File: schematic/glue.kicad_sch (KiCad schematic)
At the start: 1 part

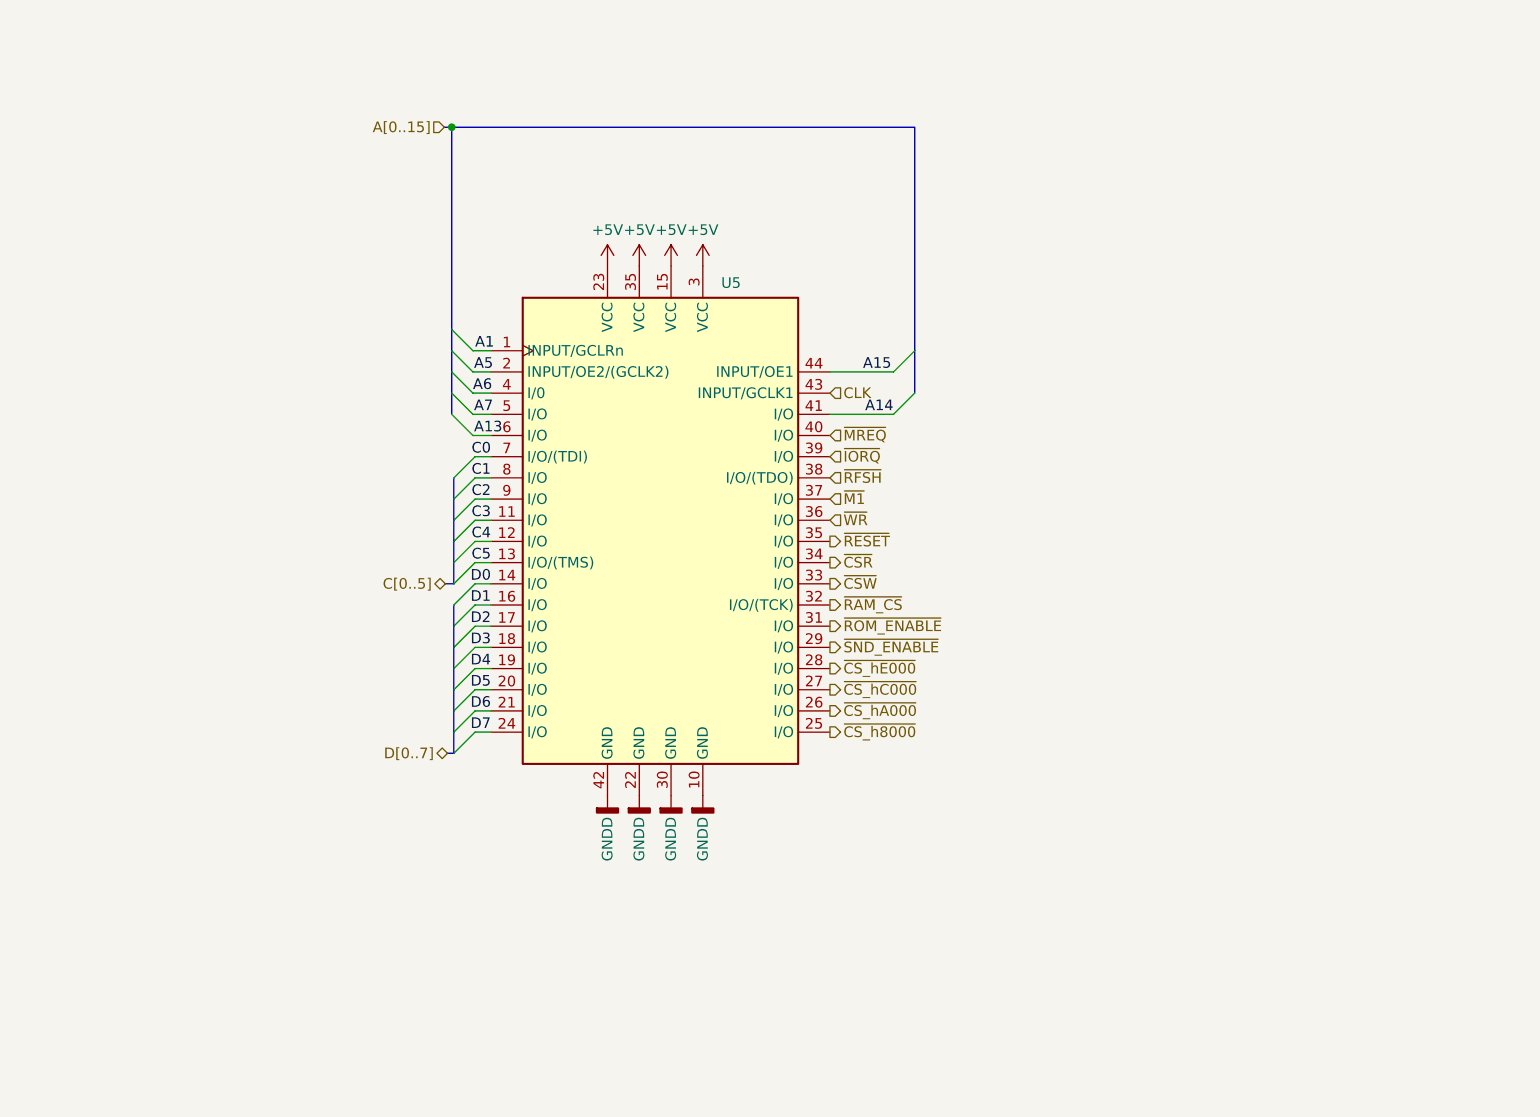
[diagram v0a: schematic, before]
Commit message: first commit of portable coleco, major changes... pcb meh. CPLD code tested, quartus build works.
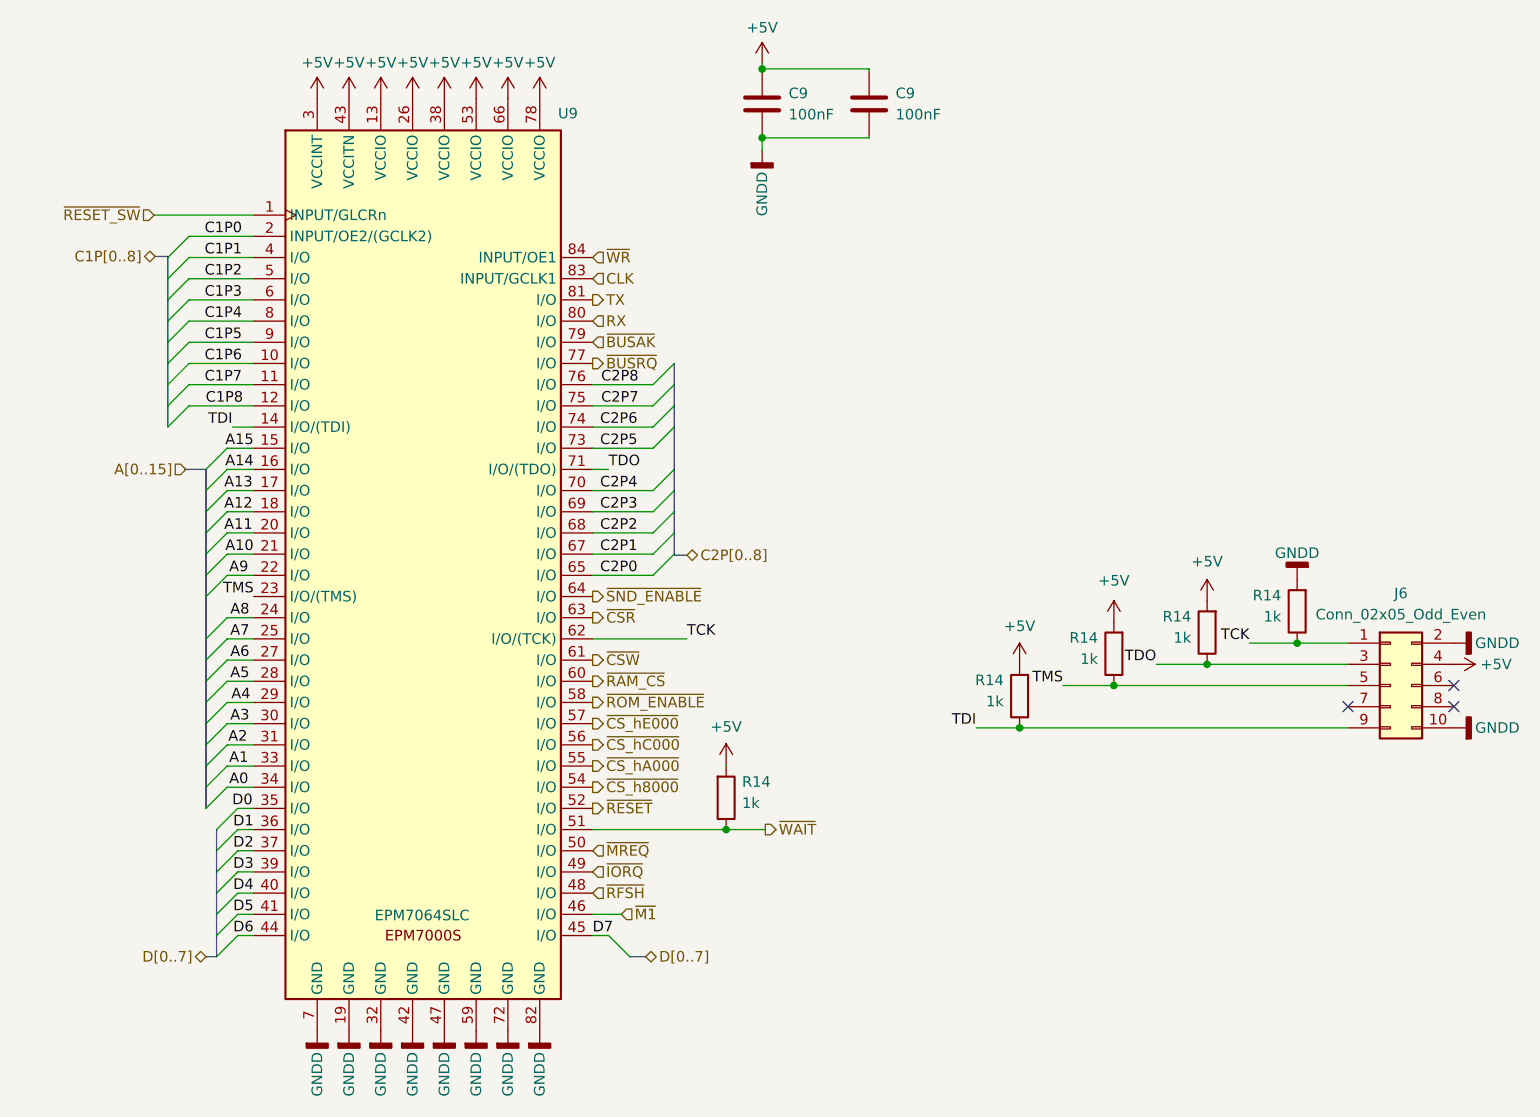
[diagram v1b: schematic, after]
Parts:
- removed U5: ~, symbol CPLD:MAX7000_44_PLC
- added C9 (x2): 100nF, Capacitor_THT:C_Disc_D7.0mm_W2.5mm_P5.00mm, symbol Device:C
- added J6: Conn_02x05_Odd_Even, Connector_PinHeader_2.54mm:PinHeader_2x05_P2.54mm_Vertical, symbol Connector_Generic:Conn_02x05_Odd_Even
- added R14 (x5): 1k, Resistor_THT:R_Axial_DIN0207_L6.3mm_D2.5mm_P10.16mm_Horizontal, symbol Device:R
- added U9: EPM7064SLC, Package_LCC:PLCC-84_THT-Socket, symbol CPLD:MAX7000_84_PLCC
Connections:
- net +5V: now also C9.1, C9.1, J6.4 (Pin_4), R14.2, R14.2, R14.2, R14.2, U9.13 (VCCIO), U9.26 (VCCIO), U9.3 (VCCINT), U9.38 (VCCIO), U9.43 (VCCITN), U9.53 (VCCIO), U9.66 (VCCIO), U9.78 (VCCIO)
- net A1: now also U9.33 (I/O)
- net A13: now also U9.17 (I/O)
- net A14: now also U9.16 (I/O)
- net A15: now also U9.15 (I/O)
- net A5: now also U9.28 (I/O)
- net A6: now also U9.27 (I/O)
- net A7: now also U9.25 (I/O)
- net CLK: now also U9.83 (INPUT/GCLK1)
- net D0: now also U9.35 (I/O)
- net D1: now also U9.36 (I/O)
- net D2: now also U9.37 (I/O)
- net D3: now also U9.39 (I/O)
- net D4: now also U9.40 (I/O)
- net D5: now also U9.41 (I/O)
- net D6: now also U9.44 (I/O)
- net D7: now also U9.45 (I/O)
- net GNDD: now also C9.2, C9.2, J6.10 (Pin_10), J6.2 (Pin_2), R14.2, U9.19 (GND), U9.32 (GND), U9.42 (GND), U9.47 (GND), U9.59 (GND), U9.7 (GND), U9.72 (GND), U9.82 (GND)
- net ~{CSR}: now also U9.63 (I/O)
- net ~{CSW}: now also U9.61 (I/O)
- net ~{CS_h8000}: now also U9.54 (I/O)
- net ~{CS_hA000}: now also U9.55 (I/O)
- net ~{CS_hC000}: now also U9.56 (I/O)
- net ~{CS_hE000}: now also U9.57 (I/O)
- net ~{IORQ}: now also U9.49 (I/O)
- net ~{M1}: now also U9.46 (I/O)
- net ~{MREQ}: now also U9.50 (I/O)
- net ~{RAM_CS}: now also U9.60 (I/O)
- net ~{RESET}: now also U9.52 (I/O)
- net ~{RFSH}: now also U9.48 (I/O)
- net ~{ROM_ENABLE}: now also U9.58 (I/O)
- net ~{SND_ENABLE}: now also U9.64 (I/O)
- net ~{WR}: now also U9.84 (INPUT/OE1)
- new net A0: U9.34 (I/O)
- new net A10: U9.21 (I/O)
- new net A11: U9.20 (I/O)
- new net A12: U9.18 (I/O)
- new net A2: U9.31 (I/O)
- new net A3: U9.30 (I/O)
- new net A4: U9.29 (I/O)
- new net A8: U9.24 (I/O)
- new net A9: U9.22 (I/O)
- new net C1P0: U9.2 (INPUT/OE2/(GCLK2))
- new net C1P1: U9.4 (I/O)
- new net C1P2: U9.5 (I/O)
- new net C1P3: U9.6 (I/O)
- new net C1P4: U9.8 (I/O)
- new net C1P5: U9.9 (I/O)
- new net C1P6: U9.10 (I/O)
- new net C1P7: U9.11 (I/O)
- new net C1P8: U9.12 (I/O)
- new net C2P0: U9.65 (I/O)
- new net C2P1: U9.67 (I/O)
- new net C2P2: U9.68 (I/O)
- new net C2P3: U9.69 (I/O)
- new net C2P4: U9.70 (I/O)
- new net C2P5: U9.73 (I/O)
- new net C2P6: U9.74 (I/O)
- new net C2P7: U9.75 (I/O)
- new net C2P8: U9.76 (I/O)
- new net RX: U9.80 (I/O)
- new net TCK: J6.1 (Pin_1), R14.1, U9.62 (I/O/(TCK))
- new net TDI: J6.9 (Pin_9), R14.1, U9.14 (I/O/(TDI))
- new net TDO: J6.3 (Pin_3), R14.1, U9.71 (I/O/(TDO))
- new net TMS: J6.5 (Pin_5), R14.1, U9.23 (I/O/(TMS))
- new net TX: U9.81 (I/O)
- new net ~{BUSAK}: U9.79 (I/O)
- new net ~{BUSRQ}: U9.77 (I/O)
- new net ~{RESET_SW}: U9.1 (INPUT/GLCRn)
- new net ~{WAIT}: R14.1, U9.51 (I/O)
- no-connect marks 0 -> 3

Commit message: first prototype board complete with smd ram
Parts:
- R14: footprint Resistor_THT:R_Axial_DIN0207_L6.3mm_D2.5mm_P10.16mm_Horizontal -> Resistor_SMD:R_0805_2012Metric
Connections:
- net C2P0: now also U9.70 (I/O); no longer U9.65 (I/O)
- net C2P1: now also U9.73 (I/O); no longer U9.67 (I/O)
- net C2P2: now also U9.74 (I/O); no longer U9.68 (I/O)
- net C2P3: now also U9.75 (I/O); no longer U9.69 (I/O)
- net C2P4: now also U9.76 (I/O); no longer U9.70 (I/O)
- net C2P5: now also U9.77 (I/O); no longer U9.73 (I/O)
- net C2P6: now also U9.79 (I/O); no longer U9.74 (I/O)
- net C2P7: now also U9.80 (I/O); no longer U9.75 (I/O)
- net C2P8: now also U9.81 (I/O); no longer U9.76 (I/O)
- net D0: now also U9.46 (I/O); no longer U9.35 (I/O)
- net D1: now also U9.48 (I/O); no longer U9.36 (I/O)
- net D2: now also U9.50 (I/O); no longer U9.37 (I/O)
- net D3: now also U9.55 (I/O); no longer U9.39 (I/O)
- net D4: now also U9.54 (I/O); no longer U9.40 (I/O)
- net D5: now also U9.52 (I/O); no longer U9.41 (I/O)
- net D6: now also U9.51 (I/O); no longer U9.44 (I/O)
- net D7: now also U9.49 (I/O); no longer U9.45 (I/O)
- net RX: now also U9.60 (I/O); no longer U9.80 (I/O)
- net TX: now also U9.61 (I/O); no longer U9.81 (I/O)
- net ~{BUSAK}: now also U9.41 (I/O); no longer U9.79 (I/O)
- net ~{BUSRQ}: now also U9.40 (I/O); no longer U9.77 (I/O)
- net ~{CSR}: now also U9.68 (I/O); no longer U9.63 (I/O)
- net ~{CSW}: now also U9.69 (I/O); no longer U9.61 (I/O)
- net ~{CS_h8000}: now also U9.65 (I/O); no longer U9.54 (I/O)
- net ~{CS_hA000}: now also U9.64 (I/O); no longer U9.55 (I/O)
- net ~{CS_hC000}: now also U9.63 (I/O); no longer U9.56 (I/O)
- net ~{CS_hE000}: now also U9.67 (I/O); no longer U9.57 (I/O)
- net ~{IORQ}: now also U9.44 (I/O); no longer U9.49 (I/O)
- net ~{M1}: now also U9.35 (I/O); no longer U9.46 (I/O)
- net ~{MREQ}: now also U9.45 (I/O); no longer U9.50 (I/O)
- net ~{RAM_CS}: now also U9.57 (I/O); no longer U9.60 (I/O)
- net ~{RESET}: now also U9.37 (I/O); no longer U9.52 (I/O)
- net ~{RFSH}: now also U9.36 (I/O); no longer U9.48 (I/O)
- net ~{ROM_ENABLE}: now also U9.56 (I/O); no longer U9.58 (I/O)
- net ~{SND_ENABLE}: now also U9.58 (I/O); no longer U9.64 (I/O)
- net ~{WAIT}: now also U9.39 (I/O); no longer U9.51 (I/O)
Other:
- moved on the sheet: R14

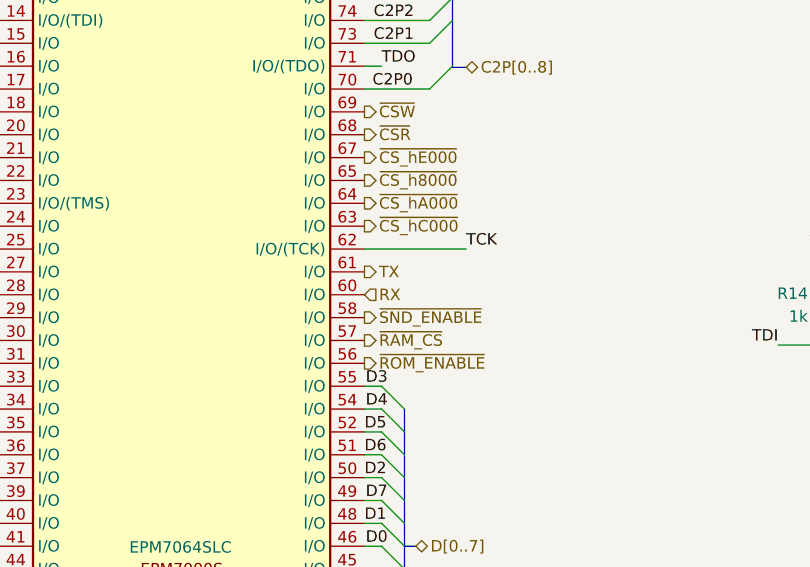
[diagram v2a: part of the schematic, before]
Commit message: moved JTAG connector over to make room for power on side of board
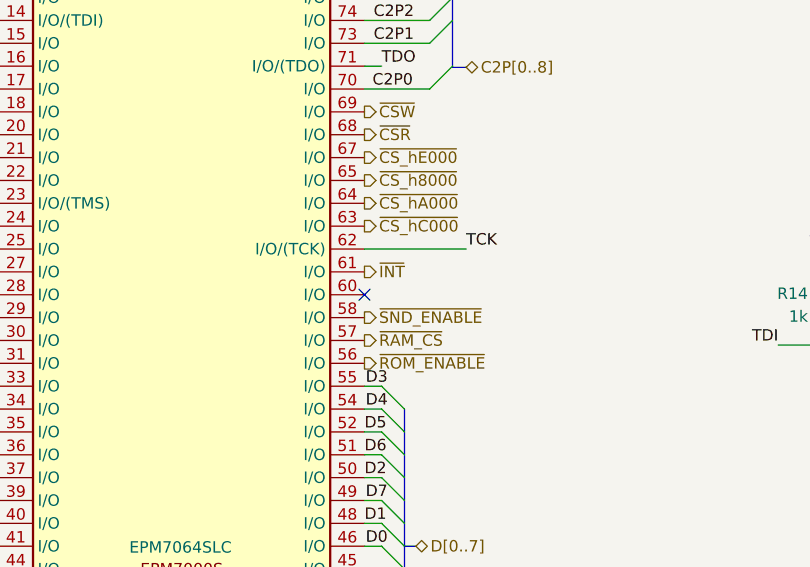
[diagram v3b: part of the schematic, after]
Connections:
- net RX: no longer names the net of U9.60 (I/O)
- net TX renamed ~{INT}
- no-connect marks 3 -> 4
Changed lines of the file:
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@@
   (junction (at 142.367 40.386) (diameter 0) (color 0 0 0 0)
   )
+  (no_connect (at 122.047 113.792))
   (no_connect (at 225.298 114.3))
   (no_connect (at 212.598 116.84))
@@
     (effects (font (size 1.27 1.27)) (justify right))
   )
-  (hierarchical_label "RX" (shape input) (at 122.047 113.792 0) (fields_autoplaced)
-    (effects (font (size 1.27 1.27)) (justify left))
-  )
   (hierarchical_label "CLK" (shape input) (at 122.047 65.532 0) (fields_autoplaced)
     (effects (font (size 1.27 1.27)) (justify left))
@@
     (effects (font (size 1.27 1.27)) (justify right))
   )
-  (hierarchical_label "TX" (shape output) (at 122.047 111.252 0) (fields_autoplaced)
-    (effects (font (size 1.27 1.27)) (justify left))
-  )
   (hierarchical_label "~{CS_hE000}" (shape output) (at 122.047 98.552 0) (fields_autoplaced)
     (effects (font (size 1.27 1.27)) (justify left))
@@
     (effects (font (size 1.27 1.27)) (justify right))
   )
+  (hierarchical_label "~{INT}" (shape output) (at 122.047 111.252 0) (fields_autoplaced)
+    (effects (font (size 1.27 1.27)) (justify left))
+  )
   (hierarchical_label "~{WAIT}" (shape output) (at 65.659 136.652 180) (fields_autoplaced)
